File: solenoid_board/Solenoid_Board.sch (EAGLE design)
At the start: 18 parts, among them Q1 MOSFET-NCHANNELSMD, Q2 MOSFET-NCHANNELSMD, Q3 MOSFET-NCHANNELSMD, Q4 MOSFET-NCHANNELSMD

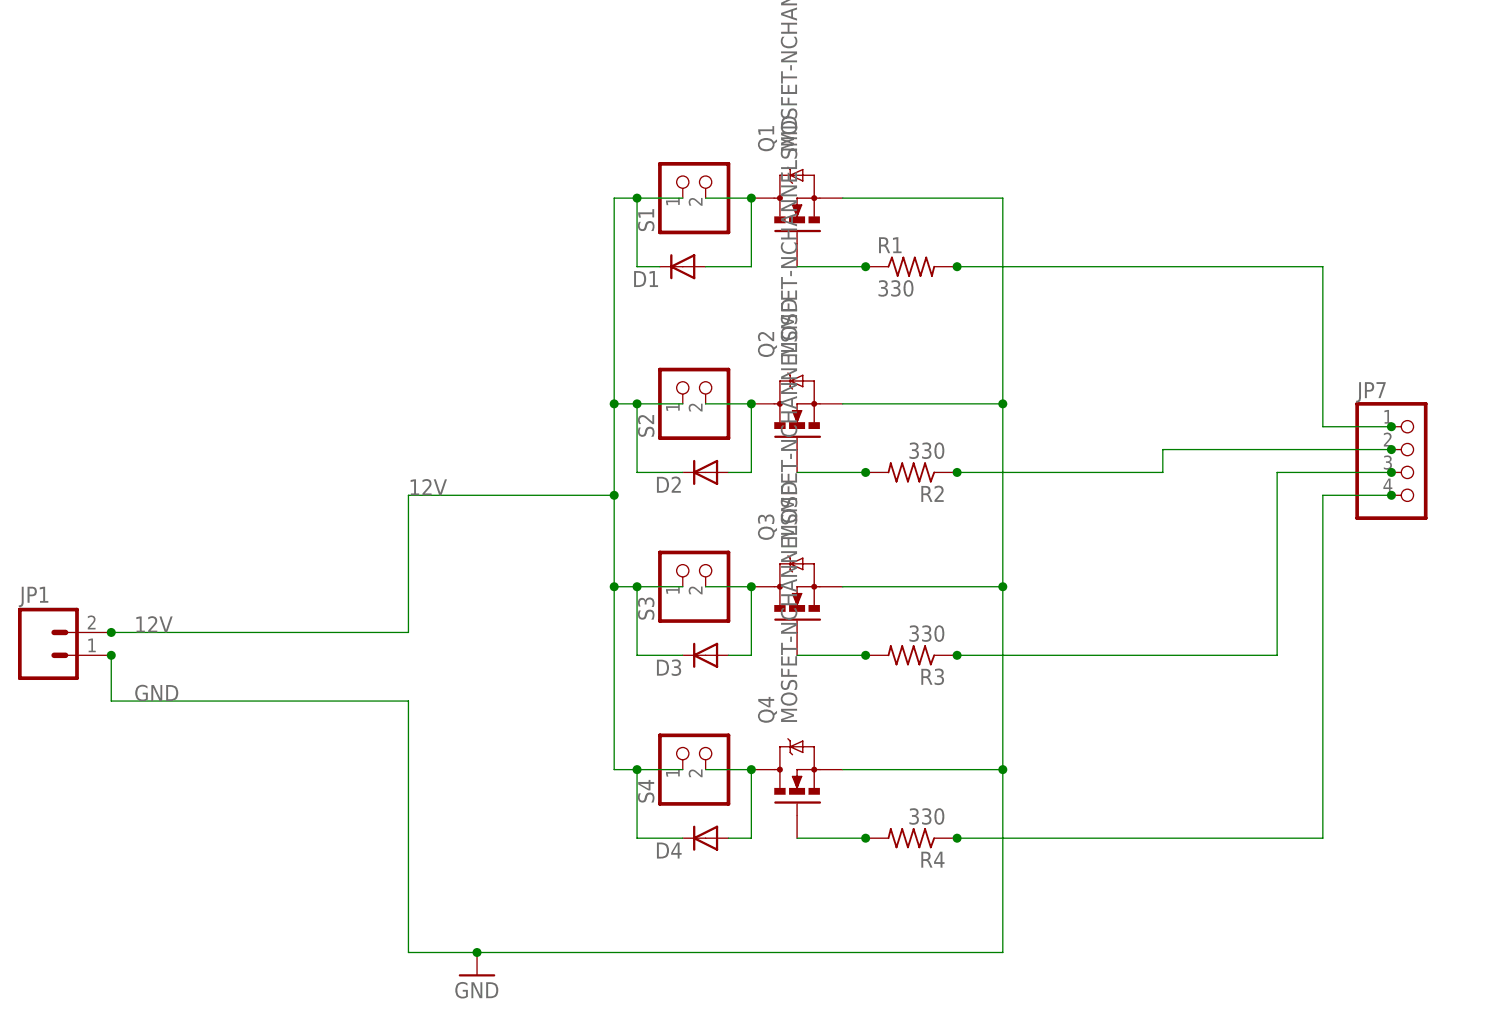
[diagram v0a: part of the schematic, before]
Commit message: Added the new connectors and finished the solenoid.
Change-Id: Ib5061dd60fbaf8b9f1d173d821b204b554eb5b3c
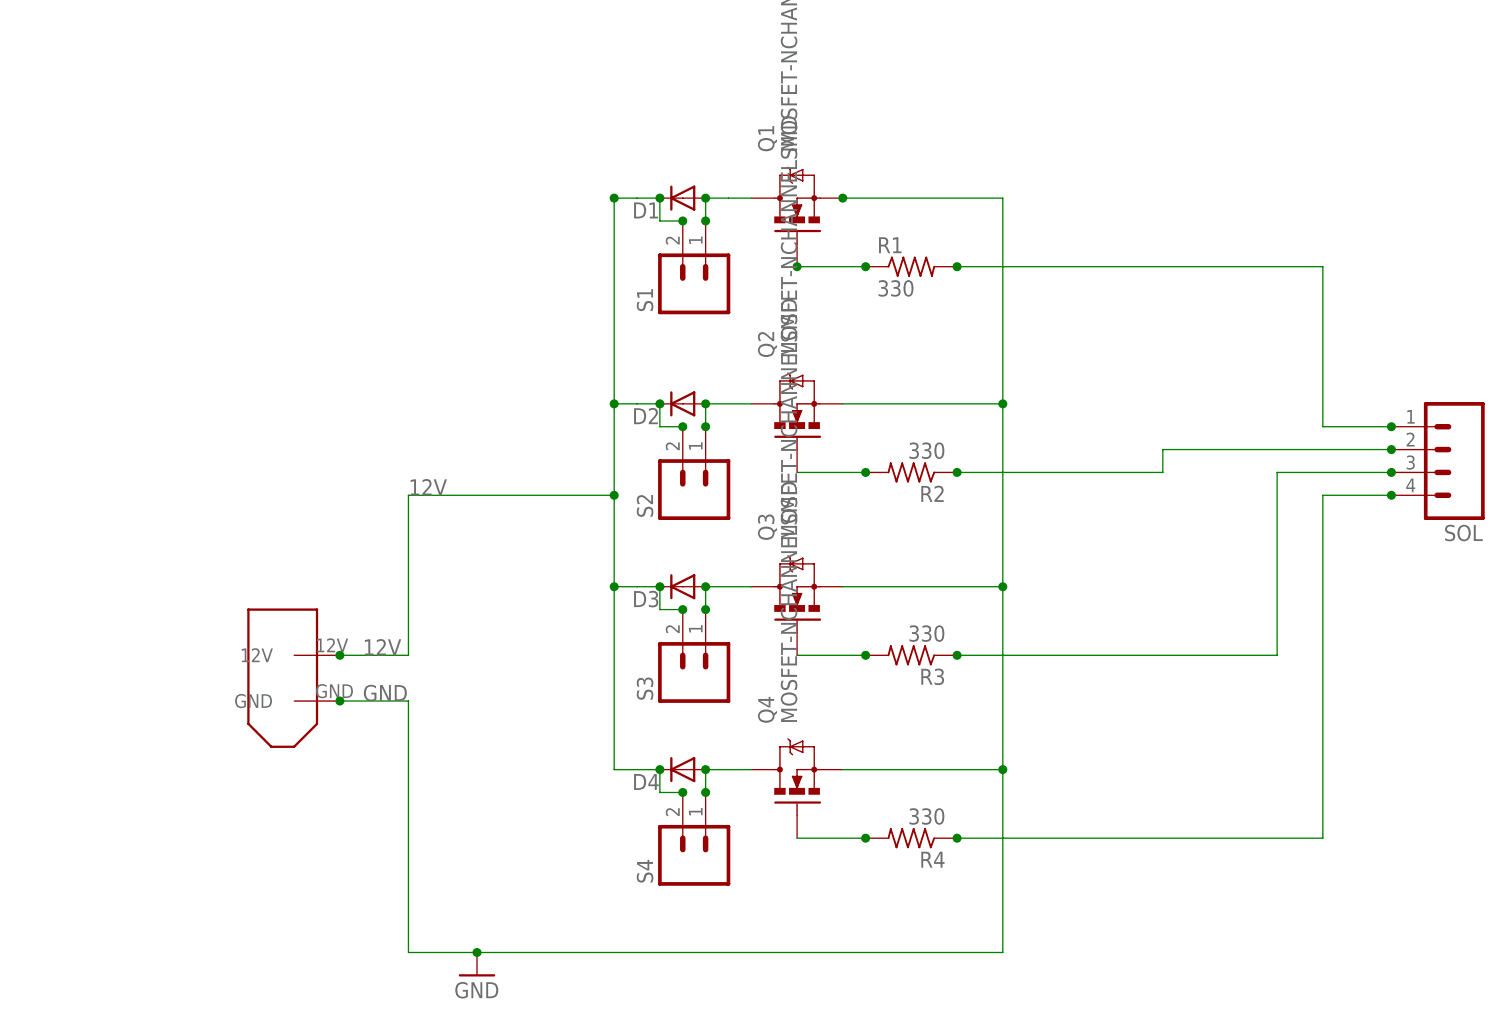
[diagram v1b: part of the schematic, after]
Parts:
- removed JP1: (no value), SparkFun:M02PTH4
- removed JP7: (no value), pinhead:PINHD-1X4
- added SOL: M04, pie:M04
- added U$2: XT60CONNECTOR, pie:XT60CONNECTOR
- S1, S2, S3, S4: value (none) -> M02; device pinhead:PINHD-1X2 -> pie:M02
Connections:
- net 12V: now also S1.2, S2.2, S3.2, S4.2, U$2.12V; no longer JP1.2, S1.1, S2.1, S3.1, S4.1
- net GND: now also U$2.GND; no longer JP1.1
- net N$1: now also SOL.1; no longer JP7.1
- net N$2: now also S1.1; no longer S1.2
- net N$3: now also S4.1; no longer S4.2
- net N$4: now also S3.1; no longer S3.2
- net N$5: now also SOL.2; no longer JP7.2
- net N$6: now also SOL.3; no longer JP7.3
- net N$7: now also SOL.4; no longer JP7.4
- net N$8: now also S2.1; no longer S2.2
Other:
- moved on the sheet: D1, D2, D3, D4, S1, S2, S3, S4

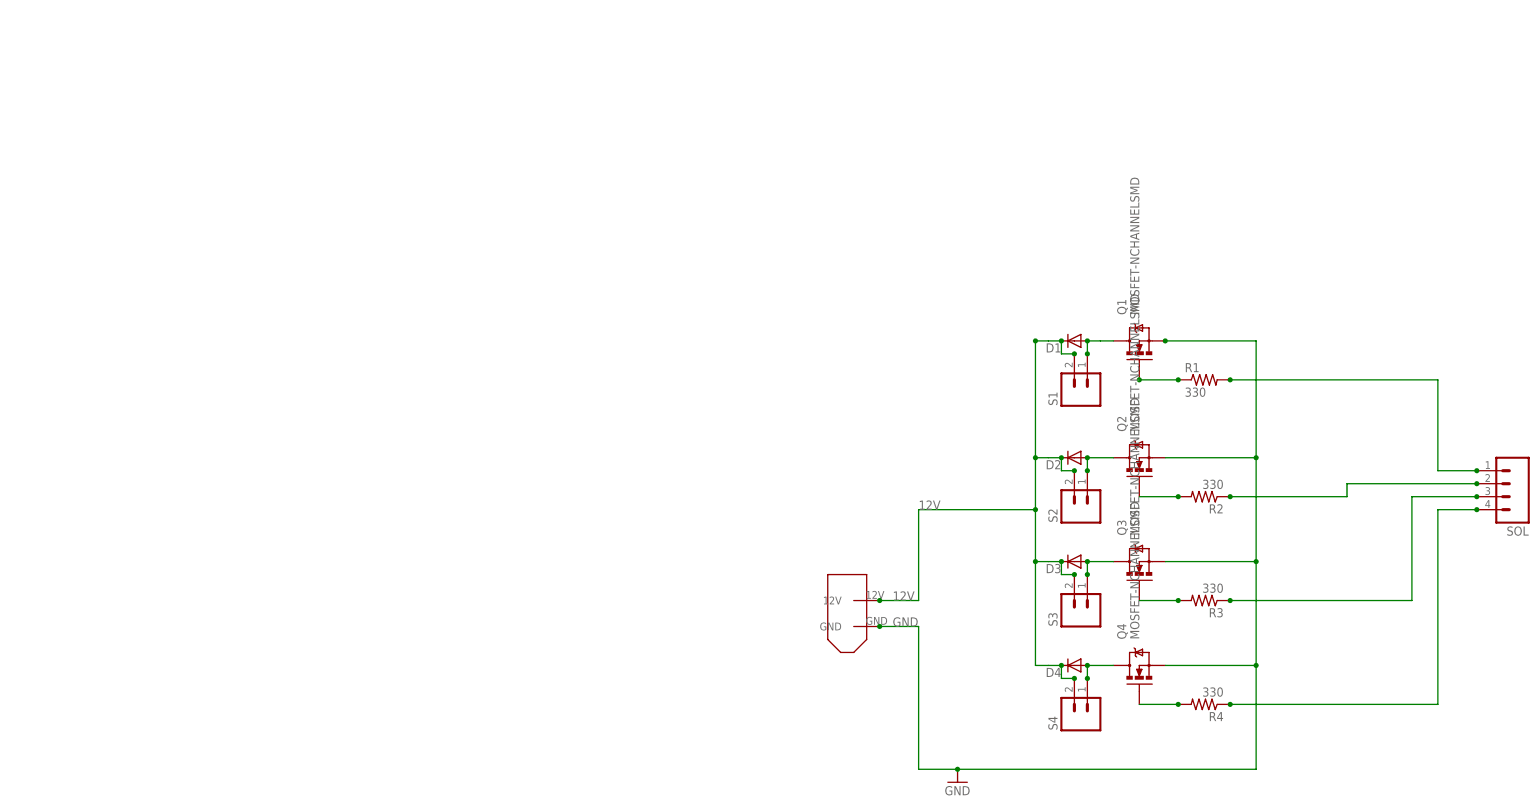
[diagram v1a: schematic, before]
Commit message: Fix all schematics to have a frame and be in quadrant I
Change-Id: I9709ffe2e940512e8f74172f888a837b658cad74
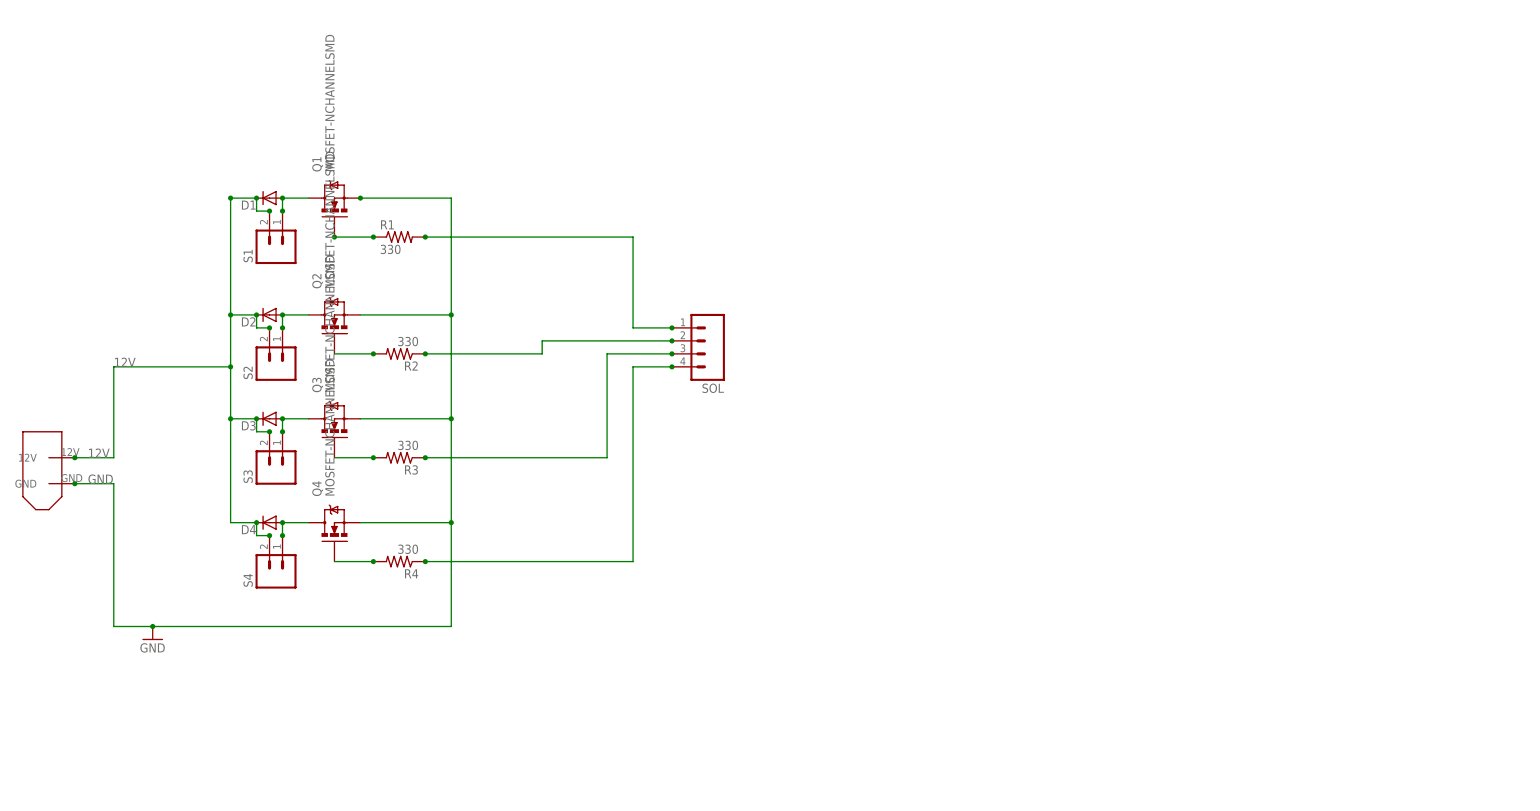
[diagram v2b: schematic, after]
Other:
- moved on the sheet: D1, D2, D3, D4, Q1, Q2, Q3, Q4, R1, R2, R3, R4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
